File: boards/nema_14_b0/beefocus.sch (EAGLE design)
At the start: 20 parts, among them J3 POWER_JACK

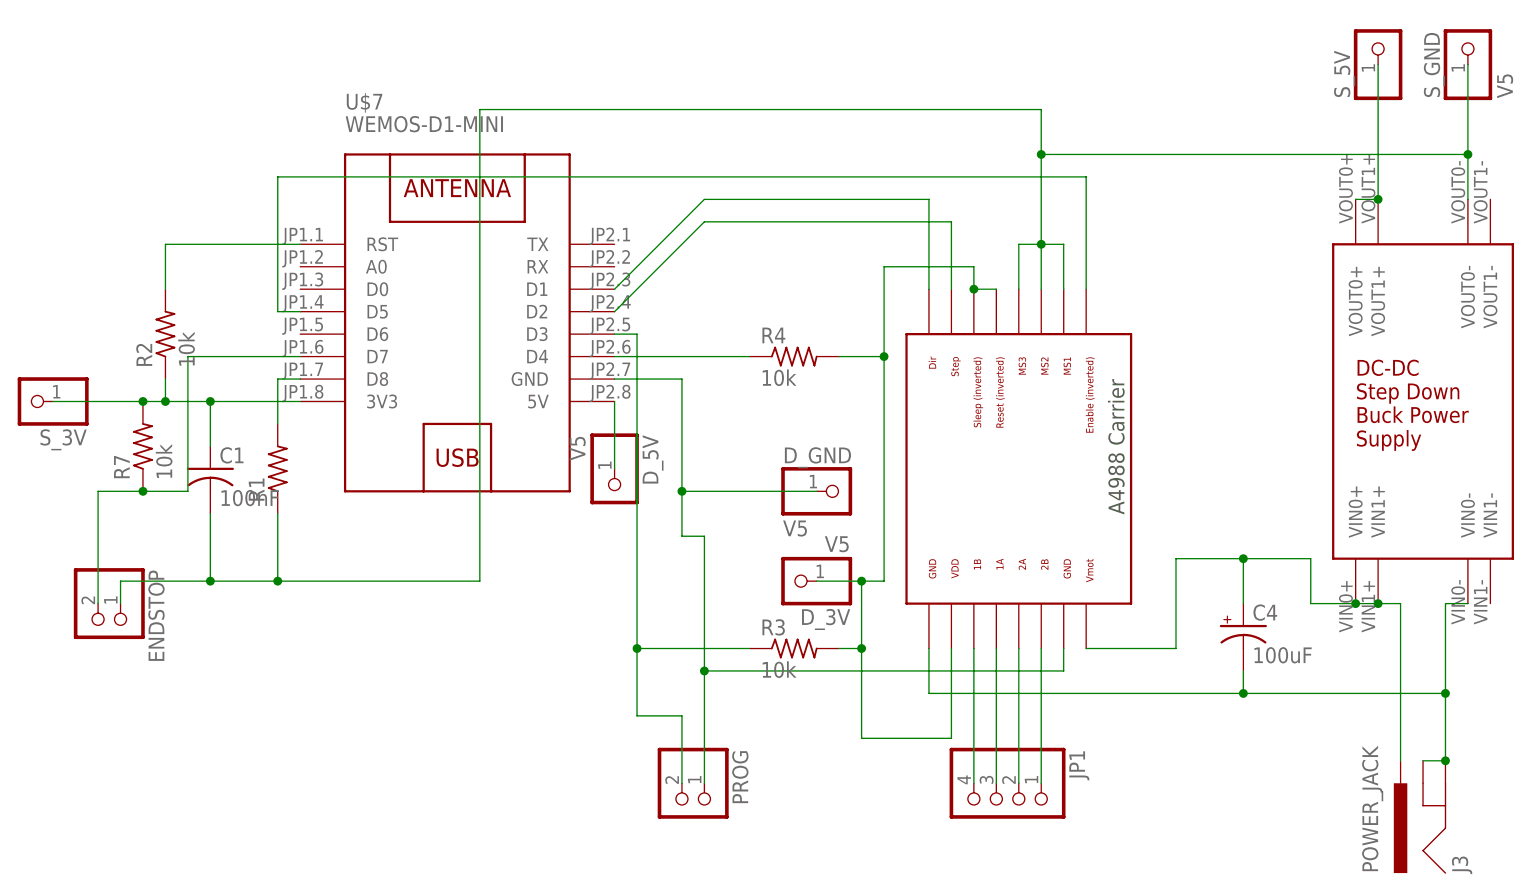
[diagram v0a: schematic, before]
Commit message: Update board to fix lost trace to ground :(
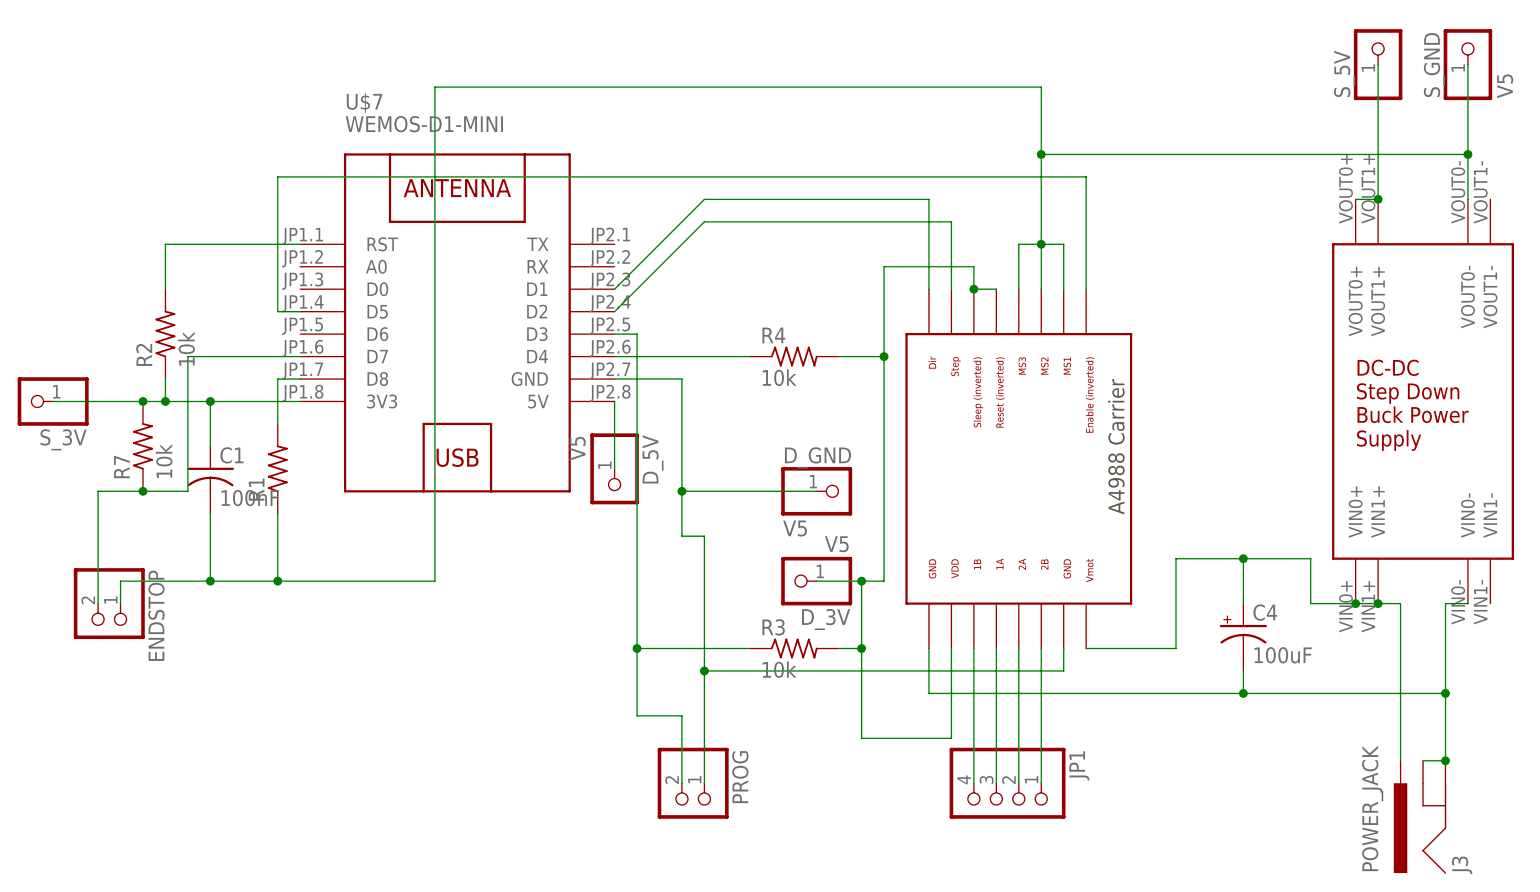
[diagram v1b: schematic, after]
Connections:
- removed net N$13: C1.2, ENDSTOP.1, R1.1
- net N$18: now also C1.2, ENDSTOP.1, R1.1
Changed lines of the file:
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@@
-</segment>
-</net>
-<net name="N$13" class="0">
-<segment>
-<pinref part="R1" gate="G$1" pin="1"/>
-<wire x1="-83.82" y1="20.32" x2="-76.2" y2="20.32" width="0.1524" layer="91"/>
-<wire x1="-76.2" y1="20.32" x2="-76.2" y2="27.94" width="0.1524" layer="91"/>
-<pinref part="ENDSTOP" gate="G$1" pin="1"/>
-<wire x1="-93.98" y1="17.78" x2="-93.98" y2="20.32" width="0.1524" layer="91"/>
-<wire x1="-93.98" y1="20.32" x2="-83.82" y2="20.32" width="0.1524" layer="91"/>
-<pinref part="C1" gate="G$1" pin="2"/>
-<wire x1="-83.82" y1="27.94" x2="-83.82" y2="20.32" width="0.1524" layer="91"/>
-<junction x="-83.82" y="20.32"/>
-<wire x1="-76.2" y1="20.32" x2="-53.34" y2="20.32" width="0.1524" layer="91"/>
-<junction x="-76.2" y="20.32"/>
-<wire x1="-53.34" y1="20.32" x2="-53.34" y2="68.58" width="0.1524" layer="91"/>
 </segment>
 </net>
@@
 <wire x1="7.62" y1="58.42" x2="10.16" y2="58.42" width="0.1524" layer="91"/>
 <wire x1="7.62" y1="58.42" x2="7.62" y2="53.34" width="0.1524" layer="91"/>
-<wire x1="10.16" y1="68.58" x2="10.16" y2="73.66" width="0.1524" layer="91"/>
+<wire x1="10.16" y1="68.58" x2="10.16" y2="76.2" width="0.1524" layer="91"/>
 <junction x="10.16" y="68.58"/>
-<wire x1="10.16" y1="73.66" x2="-53.34" y2="73.66" width="0.1524" layer="91"/>
-<wire x1="-53.34" y1="73.66" x2="-53.34" y2="68.58" width="0.1524" layer="91"/>
+<wire x1="10.16" y1="76.2" x2="-58.42" y2="76.2" width="0.1524" layer="91"/>
+<wire x1="-58.42" y1="76.2" x2="-58.42" y2="20.32" width="0.1524" layer="91"/>
+<pinref part="R1" gate="G$1" pin="1"/>
+<pinref part="ENDSTOP" gate="G$1" pin="1"/>
+<wire x1="-93.98" y1="17.78" x2="-93.98" y2="20.32" width="0.1524" layer="91"/>
+<wire x1="-93.98" y1="20.32" x2="-83.82" y2="20.32" width="0.1524" layer="91"/>
+<pinref part="C1" gate="G$1" pin="2"/>
+<wire x1="-83.82" y1="27.94" x2="-83.82" y2="20.32" width="0.1524" layer="91"/>
+<junction x="-83.82" y="20.32"/>
+<wire x1="-83.82" y1="20.32" x2="-76.2" y2="20.32" width="0.1524" layer="91"/>
+<wire x1="-76.2" y1="20.32" x2="-76.2" y2="27.94" width="0.1524" layer="91"/>
+<wire x1="-58.42" y1="20.32" x2="-76.2" y2="20.32" width="0.1524" layer="91"/>
+<junction x="-76.2" y="20.32"/>
 </segment>
 </net>

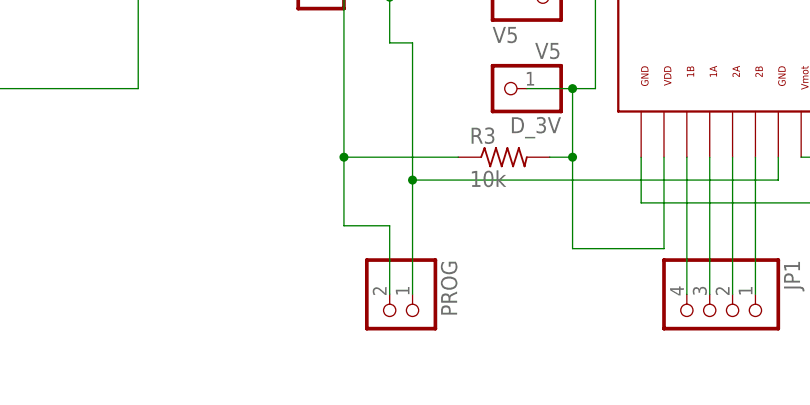
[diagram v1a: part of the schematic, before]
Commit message: Update board to take a push button switch.  This will be used to do a hard reset in the future
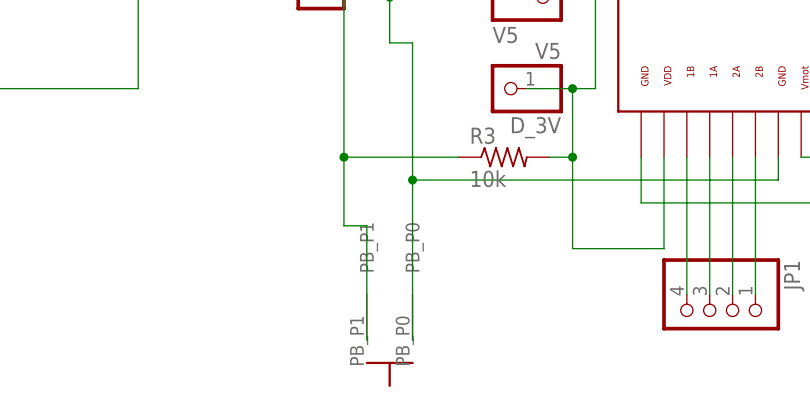
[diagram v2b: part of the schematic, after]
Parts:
- removed PROG: (no value), pinhead:PINHD-1X2/90
- added U$8: BUTTON6X6X10MMSIDE, glowmouse_custom:BUTTON6X6X10MMSIDE
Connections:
- net N$10: now also U$8.PB_P1; no longer PROG.2
- net N$16: now also U$8.PB_P0; no longer PROG.1
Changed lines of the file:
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@@
 <part name="U$1" library="RepRapjr" deviceset="POLOLU_A4983CARRIER" device=""/>
 <part name="JP1" library="pinhead" library_urn="urn:adsk.eagle:library:325" deviceset="PINHD-1X4" device="/90" package3d_urn="urn:adsk.eagle:package:22404/2"/>
-<part name="PROG" library="pinhead" library_urn="urn:adsk.eagle:library:325" deviceset="PINHD-1X2" device="/90" package3d_urn="urn:adsk.eagle:package:22437/2"/>
 <part name="ENDSTOP" library="pinhead" library_urn="urn:adsk.eagle:library:325" deviceset="PINHD-1X2" device="/90" package3d_urn="urn:adsk.eagle:package:22437/2"/>
 <part name="C4" library="resistor" library_urn="urn:adsk.eagle:library:348" deviceset="CPOL-US" device="E3.5-8" package3d_urn="urn:adsk.eagle:package:25842/1" value="100uF"/>
@@
 <part name="U$6" library="glowmouse_custom" deviceset="DCPOWERCONV" device=""/>
 <part name="U$7" library="diy-modules" deviceset="WEMOS-D1-MINI" device=""/>
+<part name="U$8" library="glowmouse_custom" deviceset="BUTTON6X6X10MMSIDE" device=""/>
 </parts>
 <sheets>
@@
 <instance part="U$1" gate="G$1" x="12.7" y="27.94" rot="R270"/>
 <instance part="JP1" gate="A" x="5.08" y="-5.08" rot="R270"/>
-<instance part="PROG" gate="G$1" x="-30.48" y="-5.08" rot="R270"/>
 <instance part="ENDSTOP" gate="G$1" x="-96.52" y="15.24" rot="R270"/>
 <instance part="C4" gate="G$1" x="33.02" y="15.24"/>
@@
 <instance part="U$6" gate="G$1" x="53.34" y="43.18"/>
 <instance part="U$7" gate="G$1" x="-55.88" y="48.26"/>
+<instance part="U$8" gate="G$1" x="-30.48" y="-7.62" rot="R180"/>
 </instances>
 <busses>
@@
 <wire x1="-35.56" y1="5.08" x2="-35.56" y2="12.7" width="0.1524" layer="91"/>
 <wire x1="-35.56" y1="12.7" x2="-35.56" y2="48.26" width="0.1524" layer="91"/>
-<wire x1="-35.56" y1="5.08" x2="-30.48" y2="5.08" width="0.1524" layer="91"/>
-<pinref part="PROG" gate="G$1" pin="2"/>
-<wire x1="-30.48" y1="5.08" x2="-30.48" y2="-2.54" width="0.1524" layer="91"/>
 <pinref part="R3" gate="G$1" pin="1"/>
 <wire x1="-22.86" y1="12.7" x2="-35.56" y2="12.7" width="0.1524" layer="91"/>
 <junction x="-35.56" y="12.7"/>
 <pinref part="U$7" gate="G$1" pin="D3"/>
+<wire x1="-35.56" y1="5.08" x2="-33.02" y2="5.08" width="0.1524" layer="91"/>
+<pinref part="U$8" gate="G$1" pin="PB_P1"/>
+<wire x1="-33.02" y1="5.08" x2="-33.02" y2="-7.62" width="0.1524" layer="91"/>
 </segment>
 </net>
@@
 <segment>
 <wire x1="-30.48" y1="43.18" x2="-38.1" y2="43.18" width="0.1524" layer="91"/>
-<pinref part="PROG" gate="G$1" pin="1"/>
-<wire x1="-27.94" y1="10.16" x2="-27.94" y2="-2.54" width="0.1524" layer="91"/>
 <pinref part="U$1" gate="G$1" pin="GND@0"/>
 <wire x1="12.7" y1="12.7" x2="12.7" y2="10.16" width="0.1524" layer="91"/>
 <wire x1="12.7" y1="10.16" x2="-27.94" y2="10.16" width="0.1524" layer="91"/>
-<junction x="-27.94" y="10.16"/>
 <wire x1="-27.94" y1="25.4" x2="-27.94" y2="10.16" width="0.1524" layer="91"/>
 <wire x1="-30.48" y1="25.4" x2="-27.94" y2="25.4" width="0.1524" layer="91"/>
@@
 <junction x="-30.48" y="30.48"/>
 <pinref part="U$7" gate="G$1" pin="GND"/>
-</segment>
-</net>
+<pinref part="U$8" gate="G$1" pin="PB_P0"/>
+<wire x1="-27.94" y1="10.16" x2="-27.94" y2="-7.62" width="0.1524" layer="91"/>
+<junction x="-27.94" y="10.16"/>
+</segment>
+</net>

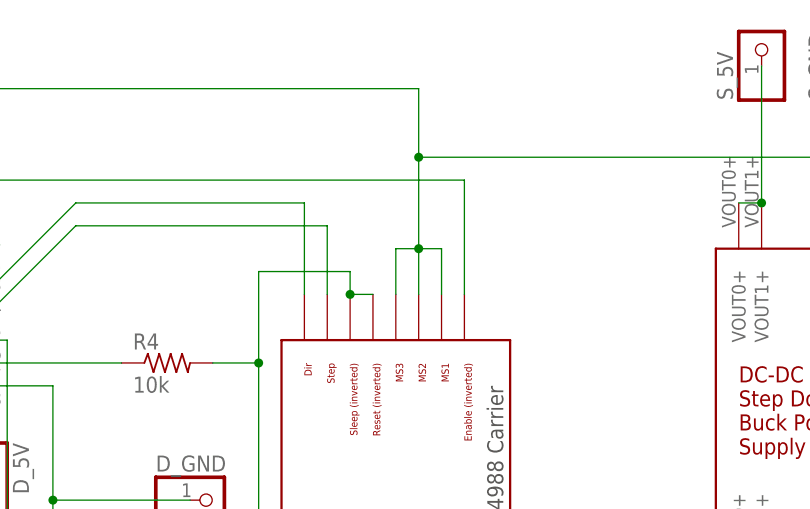
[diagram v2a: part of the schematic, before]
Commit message: Change microstepping to 1/16th on board.
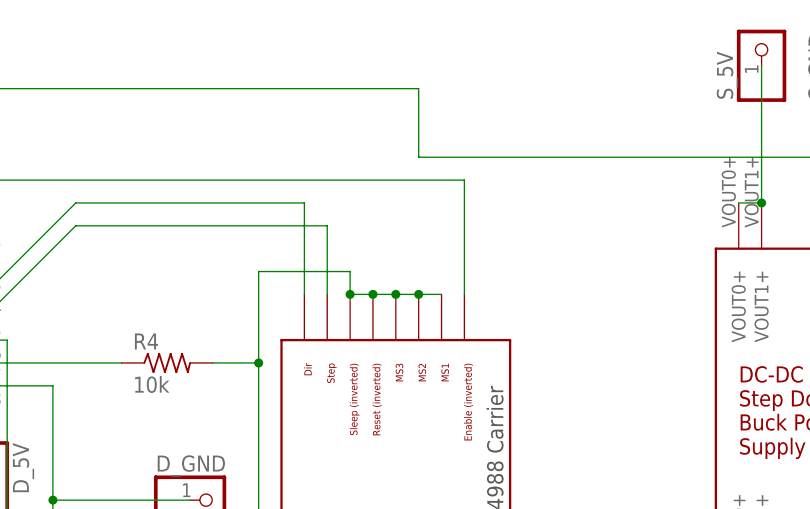
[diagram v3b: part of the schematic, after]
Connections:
- net N$17: now also U$1.MS1, U$1.MS2, U$1.MS3
- net N$18: no longer U$1.MS1, U$1.MS2, U$1.MS3
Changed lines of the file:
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@@
 <wire x1="2.54" y1="55.88" x2="2.54" y2="53.34" width="0.1524" layer="91"/>
 <junction x="2.54" y="53.34"/>
+<pinref part="U$1" gate="G$1" pin="MS3"/>
+<wire x1="5.08" y1="53.34" x2="7.62" y2="53.34" width="0.1524" layer="91"/>
+<junction x="5.08" y="53.34"/>
+<pinref part="U$1" gate="G$1" pin="MS2"/>
+<wire x1="7.62" y1="53.34" x2="10.16" y2="53.34" width="0.1524" layer="91"/>
+<junction x="7.62" y="53.34"/>
+<pinref part="U$1" gate="G$1" pin="MS1"/>
+<wire x1="10.16" y1="53.34" x2="12.7" y2="53.34" width="0.1524" layer="91"/>
+<junction x="10.16" y="53.34"/>
 </segment>
 </net>
@@
 <net name="N$18" class="0">
 <segment>
-<pinref part="U$1" gate="G$1" pin="MS3"/>
 <pinref part="U$6" gate="G$1" pin="VOUT0-"/>
 <wire x1="58.42" y1="68.58" x2="58.42" y2="63.5" width="0.1524" layer="91"/>
@@
 <junction x="58.42" y="68.58"/>
 <wire x1="10.16" y1="68.58" x2="58.42" y2="68.58" width="0.1524" layer="91"/>
-<pinref part="U$1" gate="G$1" pin="MS1"/>
-<wire x1="12.7" y1="58.42" x2="12.7" y2="53.34" width="0.1524" layer="91"/>
-<pinref part="U$1" gate="G$1" pin="MS2"/>
-<wire x1="10.16" y1="58.42" x2="10.16" y2="53.34" width="0.1524" layer="91"/>
-<wire x1="10.16" y1="58.42" x2="12.7" y2="58.42" width="0.1524" layer="91"/>
-<junction x="10.16" y="58.42"/>
-<wire x1="10.16" y1="58.42" x2="10.16" y2="68.58" width="0.1524" layer="91"/>
-<wire x1="7.62" y1="58.42" x2="10.16" y2="58.42" width="0.1524" layer="91"/>
-<wire x1="7.62" y1="58.42" x2="7.62" y2="53.34" width="0.1524" layer="91"/>
 <wire x1="10.16" y1="68.58" x2="10.16" y2="76.2" width="0.1524" layer="91"/>
-<junction x="10.16" y="68.58"/>
 <wire x1="10.16" y1="76.2" x2="-58.42" y2="76.2" width="0.1524" layer="91"/>
 <wire x1="-58.42" y1="76.2" x2="-58.42" y2="20.32" width="0.1524" layer="91"/>
